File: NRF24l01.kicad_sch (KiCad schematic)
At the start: 30 parts, among them IC1 RFX2401C, J1 SMA Connector, U4 NRF24L01, Y1 Crystal(16MHZ)

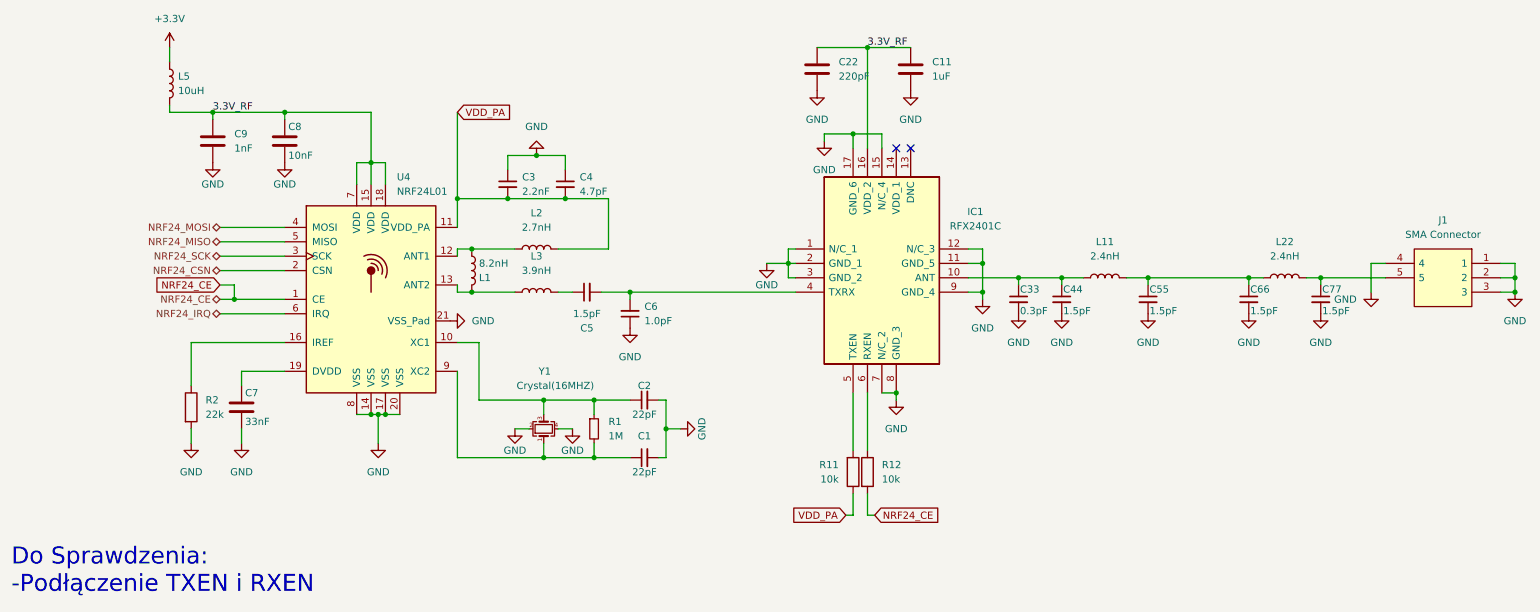
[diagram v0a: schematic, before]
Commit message: 4 layer PCB
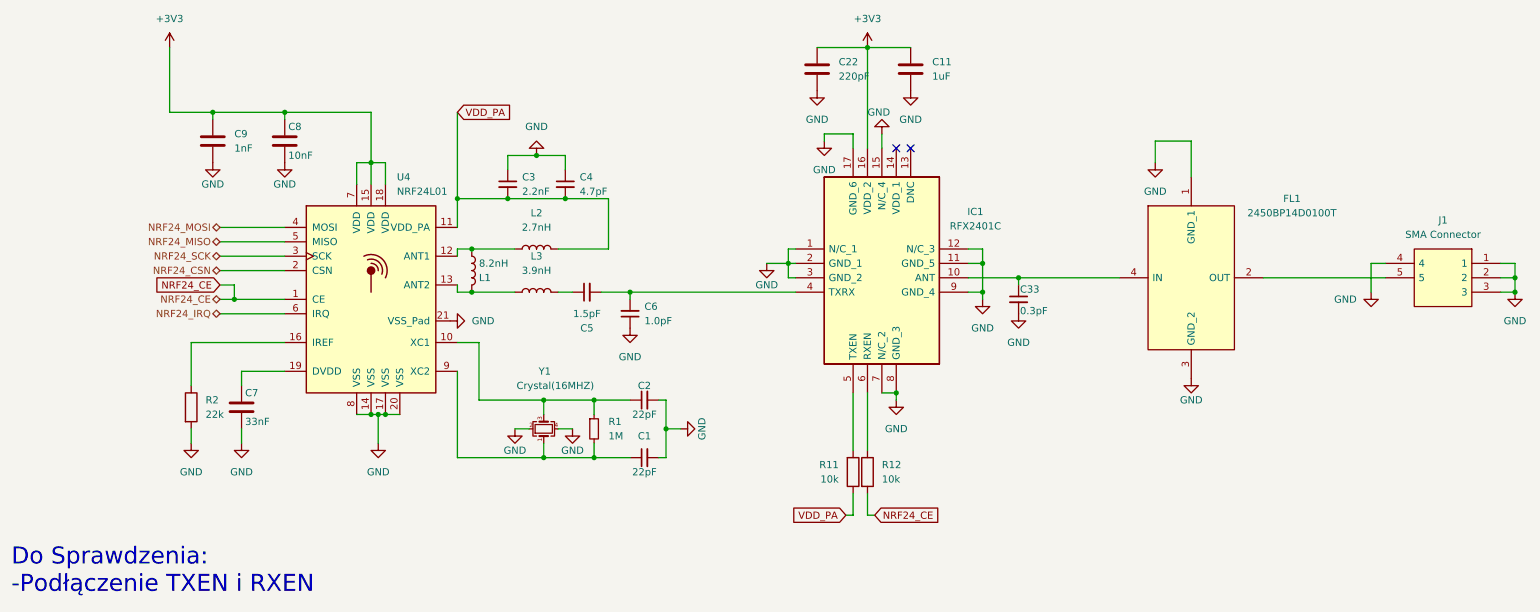
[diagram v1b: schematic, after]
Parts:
- removed C44, C55, C66, C77: 1.5pF, Capacitor_SMD:C_0402_1005Metric, symbol Device:C_Small
- removed L11, L22: 2.4nH, Inductor_SMD:L_0402_1005Metric, symbol Device:L
- removed L5: 10uH, Inductor_SMD:L_0402_1005Metric, symbol Device:L
- added FL1: 2450BP14D0100T, 2450BP14D0100T, symbol 2450BP14D0100T:2450BP14D0100T
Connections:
- net GND: now also FL1.1 (GND_1), FL1.3 (GND_2)
- net at C33.1, IC1.10 (ANT): now also FL1.4 (IN)
- net at J1.5: now also FL1.2 (OUT)
- net 3.3V_RF renamed +3V3
